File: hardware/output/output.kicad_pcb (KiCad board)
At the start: 2 copper layers, 59.5 x 100 mm, 100 parts, among them J1 AudioJack2_SwitchT, J2 AudioJack2_SwitchT, J3 AudioJack2_SwitchT, J4 AudioJack2_SwitchT, J5 Conn_02x08_Odd_Even, J6 AudioJack3, J7 Conn_02x08_Odd_Even, J8 Conn_02x08_Odd_Even, Q1 2N3906, Q2 2N3904, Q3 2N3906, Q4 2N3904, U1 TL074, U2 LM386, U3 LM386

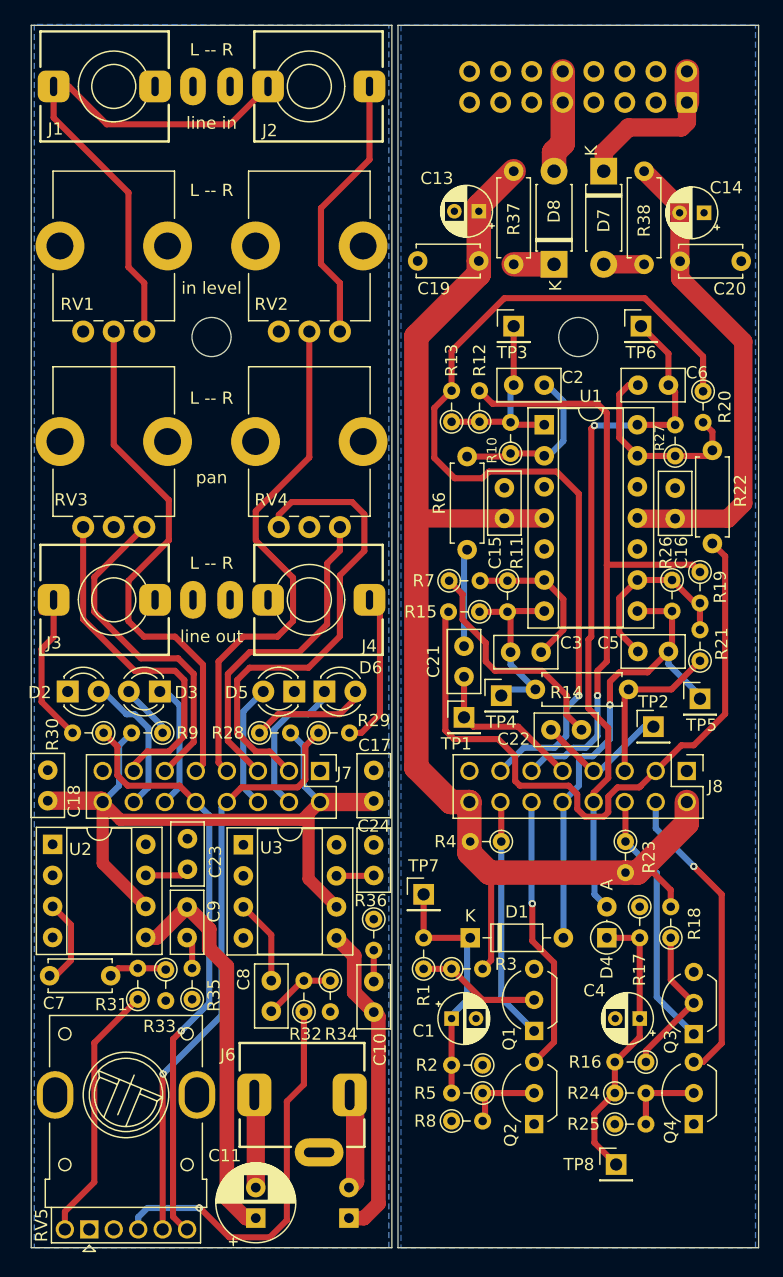
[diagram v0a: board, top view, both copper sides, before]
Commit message: v2 board: SMT components, upgraded OPA1688 amplifier
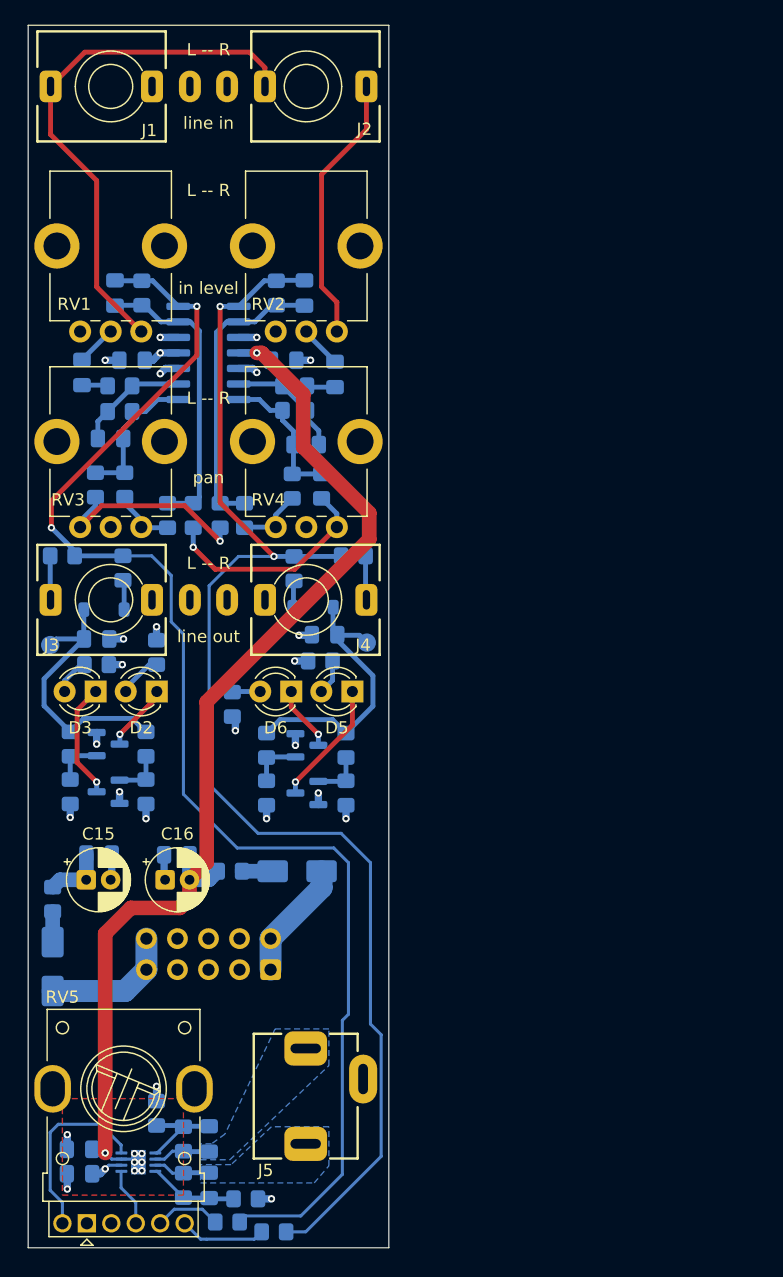
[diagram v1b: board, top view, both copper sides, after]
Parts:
- removed C19, C20: 100n, Capacitor_THT:C_Disc_D5.0mm_W2.5mm_P5.00mm
- removed C21, C22: 1u, Capacitor_THT:C_Disc_D5.0mm_W2.5mm_P2.50mm
- removed C23, C24: 100n, Capacitor_THT:C_Disc_D5.0mm_W2.5mm_P2.50mm
- removed H1, H2: MountingHole, MountingHole:MountingHole_3.2mm_M3_DIN965
- removed the J5 at (153.9, 36.3)
- removed J7, J8: Conn_02x08_Odd_Even, Custom_PinHeader_P2.54mm:PinHeader_2x08_P2.54mm_Vertical_ThinPad
- removed TP3, TP4, TP5, TP6, TP7, TP8: TestPoint, Connector_PinHeader_2.54mm:PinHeader_1x01_P2.54mm_Vertical
- removed U3: LM386, Package_DIP:DIP-8_W7.62mm_Socket
- added J6: Conn_02x05_Odd_Even, Connector_IDC:IDC-Header_2x05_P2.54mm_Vertical, B.Cu at (119.8, 107.3)
- C1: value 10u -> 1u; footprint Capacitor_THT:CP_Radial_D4.0mm_P2.00mm -> Capacitor_SMD:C_0805_2012Metric_Pad1.18x1.45mm_HandSolder; moved to B.Cu
- C10, C9: value 47n -> 100n; footprint Capacitor_THT:C_Disc_D5.0mm_W2.5mm_P2.50mm -> Capacitor_SMD:C_0805_2012Metric_Pad1.18x1.45mm_HandSolder; moved to B.Cu
- C11: value 220u -> 100n; footprint Capacitor_THT:CP_Radial_D6.3mm_P2.50mm -> Capacitor_SMD:C_0805_2012Metric_Pad1.18x1.45mm_HandSolder; moved to B.Cu
- C12: value 220u -> 100n; footprint Capacitor_THT:CP_Radial_D6.3mm_P2.50mm -> Capacitor_SMD:C_0805_2012Metric_Pad1.18x1.45mm_HandSolder
- C13, C14: value 10u -> 100n; footprint Capacitor_THT:CP_Radial_D4.0mm_P2.00mm -> Capacitor_SMD:C_0805_2012Metric_Pad1.18x1.45mm_HandSolder; moved to B.Cu
- C15, C16: value 100n -> 10u; footprint Capacitor_THT:C_Disc_D5.0mm_W2.5mm_P2.50mm -> Capacitor_THT:CP_Radial_D5.0mm_P2.00mm
- C17, C18: value 100n -> 47p; footprint Capacitor_THT:C_Disc_D5.0mm_W2.5mm_P2.50mm -> Capacitor_SMD:C_0805_2012Metric_Pad1.18x1.45mm_HandSolder; moved to B.Cu
- C2: value 22p -> 1u; footprint Capacitor_THT:C_Disc_D5.0mm_W2.5mm_P2.50mm -> Capacitor_SMD:C_0805_2012Metric_Pad1.18x1.45mm_HandSolder; moved to B.Cu
- C3, C5, C6: footprint Capacitor_THT:C_Disc_D5.0mm_W2.5mm_P2.50mm -> Capacitor_SMD:C_0805_2012Metric_Pad1.18x1.45mm_HandSolder; moved to B.Cu
- C4: value 10u -> 22p; footprint Capacitor_THT:CP_Radial_D4.0mm_P2.00mm -> Capacitor_SMD:C_0805_2012Metric_Pad1.18x1.45mm_HandSolder; moved to B.Cu
- C7: value 1u -> 10u; footprint Capacitor_THT:C_Disc_D5.0mm_W2.5mm_P5.00mm -> Capacitor_SMD:C_0805_2012Metric_Pad1.18x1.45mm_HandSolder; moved to B.Cu
- C8: value 1u -> 10u; footprint Capacitor_THT:C_Disc_D5.0mm_W2.5mm_P2.50mm -> Capacitor_SMD:C_0805_2012Metric_Pad1.18x1.45mm_HandSolder; moved to B.Cu
- D1: value 1N4148 -> 1N4148W; footprint Diode_THT:D_DO-35_SOD27_P7.62mm_Horizontal -> Diode_SMD:D_SOD-123; moved to B.Cu
- D2, D5: value GREEN -> RED
- D3, D6: value RED -> GREEN
- D4: value 1N4148 -> 1N4148W; footprint Diode_THT:D_DO-35_SOD27_P2.54mm_Vertical_AnodeUp -> Diode_SMD:D_SOD-123; moved to B.Cu
- D7, D8: value D_Schottky -> B140-E3; footprint Diode_THT:D_DO-41_SOD81_P7.62mm_Horizontal -> Diode_SMD:D_SMA; moved to B.Cu
- J1, J2, J3, J4: footprint AudioJacks:Jack_3.5mm_QingPu_WQP-PJ301M-12_Vertical -> AudioJacks:Jack_3.5mm_QingPu_WQP-PJ301M-12_Vertical_Slim
- Q1, Q3: value 2N3906 -> BC847; footprint Package_TO_SOT_THT:TO-92_Inline_Wide -> Package_TO_SOT_SMD:SOT-23; moved to B.Cu
- Q2, Q4: value 2N3904 -> BC847; footprint Package_TO_SOT_THT:TO-92_Inline_Wide -> Package_TO_SOT_SMD:SOT-23; moved to B.Cu
- R1, R12, R20, R23, R5, R7: footprint Resistor_THT:R_Axial_DIN0204_L3.6mm_D1.6mm_P2.54mm_Vertical -> Resistor_SMD:R_0805_2012Metric_Pad1.20x1.40mm_HandSolder; moved to B.Cu
- R10, R11: value 220k -> 100k; footprint Resistor_THT:R_Axial_DIN0204_L3.6mm_D1.6mm_P2.54mm_Vertical -> Resistor_SMD:R_0805_2012Metric_Pad1.20x1.40mm_HandSolder; moved to B.Cu
- R13: value 100k -> 330k; footprint Resistor_THT:R_Axial_DIN0204_L3.6mm_D1.6mm_P2.54mm_Vertical -> Resistor_SMD:R_0805_2012Metric_Pad1.20x1.40mm_HandSolder; moved to B.Cu
- R14: value 100k -> 330k; footprint Resistor_THT:R_Axial_DIN0207_L6.3mm_D2.5mm_P7.62mm_Horizontal -> Resistor_SMD:R_0805_2012Metric_Pad1.20x1.40mm_HandSolder; moved to B.Cu
- R15, R16: value 100k -> 150k; footprint Resistor_THT:R_Axial_DIN0204_L3.6mm_D1.6mm_P2.54mm_Vertical -> Resistor_SMD:R_0805_2012Metric_Pad1.20x1.40mm_HandSolder; moved to B.Cu
- R17: value 47k -> 1k; footprint Resistor_THT:R_Axial_DIN0204_L3.6mm_D1.6mm_P2.54mm_Vertical -> Resistor_SMD:R_0805_2012Metric_Pad1.20x1.40mm_HandSolder; moved to B.Cu
- R18: value 2M2 -> 1k; footprint Resistor_THT:R_Axial_DIN0204_L3.6mm_D1.6mm_P2.54mm_Vertical -> Resistor_SMD:R_0805_2012Metric_Pad1.20x1.40mm_HandSolder; moved to B.Cu
- R19: value 100k -> 1k; footprint Resistor_THT:R_Axial_DIN0204_L3.6mm_D1.6mm_P2.54mm_Vertical -> Resistor_SMD:R_0805_2012Metric_Pad1.20x1.40mm_HandSolder; moved to B.Cu
- R2: value 47k -> 100k; footprint Resistor_THT:R_Axial_DIN0204_L3.6mm_D1.6mm_P2.54mm_Vertical -> Resistor_SMD:R_0805_2012Metric_Pad1.20x1.40mm_HandSolder; moved to B.Cu
- R21, R24, R31: value 100k -> 22k; footprint Resistor_THT:R_Axial_DIN0204_L3.6mm_D1.6mm_P2.54mm_Vertical -> Resistor_SMD:R_0805_2012Metric_Pad1.20x1.40mm_HandSolder; moved to B.Cu
- R22: value 100k -> 47k; footprint Resistor_THT:R_Axial_DIN0207_L6.3mm_D2.5mm_P7.62mm_Horizontal -> Resistor_SMD:R_0805_2012Metric_Pad1.20x1.40mm_HandSolder; moved to B.Cu
- R25: value 15k -> 10k; footprint Resistor_THT:R_Axial_DIN0204_L3.6mm_D1.6mm_P2.54mm_Vertical -> Resistor_SMD:R_0805_2012Metric_Pad1.20x1.40mm_HandSolder; moved to B.Cu
- R26: value 330k -> 1k; footprint Resistor_THT:R_Axial_DIN0204_L3.6mm_D1.6mm_P2.54mm_Vertical -> Resistor_SMD:R_0805_2012Metric_Pad1.20x1.40mm_HandSolder; moved to B.Cu
- R27: value 330k -> 100k; footprint Resistor_THT:R_Axial_DIN0204_L3.6mm_D1.6mm_P2.54mm_Vertical -> Resistor_SMD:R_0805_2012Metric_Pad1.20x1.40mm_HandSolder; moved to B.Cu
- R28: value 10k -> 22k; footprint Resistor_THT:R_Axial_DIN0204_L3.6mm_D1.6mm_P2.54mm_Vertical -> Resistor_SMD:R_0805_2012Metric_Pad1.20x1.40mm_HandSolder; moved to B.Cu
- R29: value 1k -> 47k; footprint Resistor_THT:R_Axial_DIN0204_L3.6mm_D1.6mm_P2.54mm_Vertical -> Resistor_SMD:R_0805_2012Metric_Pad1.20x1.40mm_HandSolder; moved to B.Cu
- R3: value 2M2 -> 220k; footprint Resistor_THT:R_Axial_DIN0204_L3.6mm_D1.6mm_P2.54mm_Vertical -> Resistor_SMD:R_0805_2012Metric_Pad1.20x1.40mm_HandSolder; moved to B.Cu
- R30: value 1k -> 10k; footprint Resistor_THT:R_Axial_DIN0204_L3.6mm_D1.6mm_P2.54mm_Vertical -> Resistor_SMD:R_0805_2012Metric_Pad1.20x1.40mm_HandSolder; moved to B.Cu
- R32: value 100k -> 10k; footprint Resistor_THT:R_Axial_DIN0204_L3.6mm_D1.6mm_P2.54mm_Vertical -> Resistor_SMD:R_0805_2012Metric_Pad1.20x1.40mm_HandSolder; moved to B.Cu
- R33, R34: value 4k7 -> 10; footprint Resistor_THT:R_Axial_DIN0204_L3.6mm_D1.6mm_P2.54mm_Vertical -> Resistor_SMD:R_0805_2012Metric_Pad1.20x1.40mm_HandSolder; moved to B.Cu
- R35: value 10 -> 0R0; footprint Resistor_THT:R_Axial_DIN0204_L3.6mm_D1.6mm_P2.54mm_Vertical -> Resistor_SMD:R_0805_2012Metric_Pad1.20x1.40mm_HandSolder; moved to B.Cu
- R36: value 10 -> 1k0; footprint Resistor_THT:R_Axial_DIN0204_L3.6mm_D1.6mm_P2.54mm_Vertical -> Resistor_SMD:R_0805_2012Metric_Pad1.20x1.40mm_HandSolder; moved to B.Cu
- R37: value 10 -> 0R0; footprint Resistor_THT:R_Axial_DIN0207_L6.3mm_D2.5mm_P7.62mm_Horizontal -> Resistor_SMD:R_0805_2012Metric_Pad1.20x1.40mm_HandSolder; moved to B.Cu
- R38: value 10 -> 1k0; footprint Resistor_THT:R_Axial_DIN0207_L6.3mm_D2.5mm_P7.62mm_Horizontal -> Resistor_SMD:R_0805_2012Metric_Pad1.20x1.40mm_HandSolder; moved to B.Cu
- R4: value 10k -> 220k; footprint Resistor_THT:R_Axial_DIN0204_L3.6mm_D1.6mm_P2.54mm_Vertical -> Resistor_SMD:R_0805_2012Metric_Pad1.20x1.40mm_HandSolder; moved to B.Cu
- R6: footprint Resistor_THT:R_Axial_DIN0207_L6.3mm_D2.5mm_P7.62mm_Horizontal -> Resistor_SMD:R_0805_2012Metric_Pad1.20x1.40mm_HandSolder; moved to B.Cu
- R8: value 15k -> 100k; footprint Resistor_THT:R_Axial_DIN0204_L3.6mm_D1.6mm_P2.54mm_Vertical -> Resistor_SMD:R_0805_2012Metric_Pad1.20x1.40mm_HandSolder; moved to B.Cu
- R9: value 10k -> 100k; footprint Resistor_THT:R_Axial_DIN0204_L3.6mm_D1.6mm_P2.54mm_Vertical -> Resistor_SMD:R_0805_2012Metric_Pad1.20x1.40mm_HandSolder; moved to B.Cu
- TP1, TP2: footprint Connector_PinHeader_2.54mm:PinHeader_1x01_P2.54mm_Vertical -> TestPoint:TestPoint_Pad_D1.5mm; moved to B.Cu
- U1: footprint Package_DIP:DIP-14_W7.62mm_Socket -> Package_SO:SOIC-14_3.9x8.7mm_P1.27mm; moved to B.Cu
- U2: value LM386 -> OPA1688IDRG; footprint Package_DIP:DIP-8_W7.62mm_Socket -> Package_SON:WSON-8-1EP_3x3mm_P0.5mm_EP1.2x2mm; moved to B.Cu
- moved R38 86.8 mm to (110.5, 119.0), turned to 90 degrees
- moved R37 83.6 mm to (112.7, 121.1), turned to 90 degrees
- moved D7 79.2 mm to (102.0, 107.0)
- moved C14 68.0 mm to (112.2, 97.9)
- moved C13 61.1 mm to (105.8, 97.8)
- moved C1 60.9 mm to (104.4, 58.4), turned to -90 degrees
- moved R20 59.3 mm to (103.4, 88.8), turned to 90 degrees
- moved R5 57.7 mm to (107.9, 67.6), turned to -90 degrees
- moved R2 57.7 mm to (121.8, 59.5)
- moved R25 56.7 mm to (105.6, 82.3), turned to 180 degrees
- moved R17 55.3 mm to (102.8, 73.4), turned to 180 degrees
- moved C4 54.3 mm to (122.7, 64.3)
- moved R15 54.0 mm to (116.3, 127.9)
- moved D8 53.9 mm to (122.0, 99.2), turned to 180 degrees
- moved C10 53.8 mm to (120.9, 57.4), turned to 0 degrees
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- renumbered J6 to J5
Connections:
- C1 pad 1: Net-(D1-K) -> Net-(C1-Pad1)
- C1 pad 2: GND -> Net-(C1-Pad2)
- C10 pad 1: Net-(C10-Pad1) -> -12V
- C10 pad 2: Net-(C10-Pad2) -> GND
- C11 pad 1: Net-(C11-Pad1) -> GND
- C11 pad 2: Net-(C11-Pad2) -> +12V
- C12 pad 1: Net-(C10-Pad1) -> -12V
- C12 pad 2: Net-(C12-Pad2) -> GND
- C13 pad 1: +12V -> GND
- C13 pad 2: GND -> +12V
- C14 pad 1: GND -> -12V
- C14 pad 2: -12V -> GND
- C15 pad 1: GND -> +12V
- C15 pad 2: +12V -> GND
- C16 pad 1: -12V -> GND
- C16 pad 2: GND -> -12V
- C17 pad 1: GND -> Net-(U2A--)
- C17 pad 2: +12V -> /L_HP_OUT
- C18 pad 1: GND -> Net-(U2B--)
- C18 pad 2: +12V -> /R_HP_OUT
- C2 pad 1: Net-(U1A--) -> Net-(C2-Pad1)
- C3 pad 1: Net-(U1B--) -> Net-(U1A--)
- C4 pad 1: Net-(D4-K) -> Net-(U1D--)
- C4 pad 2: GND -> Net-(C4-Pad2)
- C5 pad 1: Net-(U1C--) -> Net-(U1B--)
- C5 pad 2: L_LINE_OUT_B -> /L_LINE_OUT
- C6 pad 1: Net-(U1D--) -> Net-(U1C--)
- C6 pad 2: R_LINE_OUT_B -> /R_LINE_OUT
- C7 pad 1: Net-(U2-+) -> GND
- C7 pad 2: Net-(C7-Pad2) -> Net-(D1-K)
- C8 pad 1: Net-(U3-+) -> GND
- C8 pad 2: Net-(C8-Pad2) -> Net-(D4-K)
- C9 pad 1: Net-(C11-Pad1) -> GND
- C9 pad 2: Net-(C9-Pad2) -> +12V
- D1 pad 2: L_LINE_OUT_B -> Net-(D1-A)
- D2 pad 1: GND -> Net-(D2-K)
- D2 pad 2: L_LVL_G_LED_A -> Net-(D2-A)
- D3 pad 1: L_LVL_R_LED_A -> Net-(D3-K)
- D4 pad 2: R_LINE_OUT_B -> Net-(D4-A)
- D5 pad 1: GND -> Net-(D5-K)
- D5 pad 2: R_LVL_G_LED_A -> Net-(D5-A)
- D6 pad 1: R_LVL_R_LED_A -> Net-(D6-K)
- J5 pad R: Net-(C12-Pad2) -> /R_HP_OUT
- J5 pad T: Net-(C11-Pad2) -> /L_HP_OUT
- Q1 pad 1: L_LVL_G_LED_B -> Net-(Q1-B)
- Q1 pad 2: Net-(Q1-B) -> GND
- Q1 pad 3: GND -> Net-(D2-K)
- Q2 pad 1: GND -> Net-(Q2-B)
- Q2 pad 2: Net-(Q2-B) -> GND
- Q2 pad 3: L_LVL_R_LED_B -> Net-(D3-K)
- Q3 pad 1: R_LVL_G_LED_B -> Net-(Q3-B)
- Q3 pad 2: Net-(Q3-B) -> GND
- Q3 pad 3: GND -> Net-(D5-K)
- Q4 pad 1: GND -> Net-(Q4-B)
- Q4 pad 2: Net-(Q4-B) -> GND
- Q4 pad 3: R_LVL_R_LED_B -> Net-(D6-K)
- R1 pad 1: Net-(Q1-B) -> Net-(C1-Pad2)
- R1 pad 2: Net-(D1-K) -> Net-(U1A--)
- R10 pad 1: Net-(U1A--) -> Net-(R10-Pad1)
- R10 pad 2: Net-(C2-Pad2) -> Net-(U1C--)
- R11 pad 1: Net-(U1B--) -> Net-(R11-Pad1)
- R11 pad 2: Net-(C3-Pad2) -> Net-(U1B--)
- R12 pad 1: Net-(C2-Pad2) -> Net-(R12-Pad1)
- R12 pad 2: L_PAN_1_B -> Net-(U1C--)
- R13 pad 1: Net-(C2-Pad2) -> Net-(U1B--)
- R13 pad 2: L_PAN_2_B -> /L_LINE_OUT
- R14 pad 1: Net-(C3-Pad2) -> Net-(U1C--)
- R14 pad 2: R_PAN_1_B -> /R_LINE_OUT
- R15 pad 1: Net-(C3-Pad2) -> /L_LINE_OUT
- R15 pad 2: R_PAN_2_B -> Net-(R15-Pad2)
- R16 pad 1: Net-(Q3-B) -> /R_LINE_OUT
- R16 pad 2: Net-(D4-K) -> Net-(R16-Pad2)
- R17 pad 1: GND -> /L_LINE_OUT
- R17 pad 2: Net-(D4-K) -> Net-(J3-PadT)
- R18 pad 1: Net-(Q3-B) -> /R_LINE_OUT
- R18 pad 2: +12V -> Net-(J4-PadT)
- R19 pad 1: L_PAN_1_B -> Net-(D1-A)
- R19 pad 2: Net-(U1C--) -> /L_LINE_OUT
- R2 pad 1: GND -> Net-(C2-Pad2)
- R2 pad 2: Net-(D1-K) -> Net-(U1D--)
- R20 pad 1: L_PAN_2_B -> Net-(Q1-B)
- R20 pad 2: Net-(U1D--) -> Net-(D1-K)
- R21 pad 1: R_PAN_1_B -> GND
- R21 pad 2: Net-(U1C--) -> Net-(Q1-B)
- R22 pad 1: R_PAN_2_B -> Net-(Q2-B)
- R22 pad 2: Net-(U1D--) -> Net-(D1-K)
- R23 pad 1: R_LVL_G_LED_B -> +12V
- R23 pad 2: +12V -> Net-(D2-A)
- R24 pad 1: Net-(D4-K) -> GND
- R24 pad 2: Net-(Q4-B) -> Net-(Q2-B)
- R25 pad 1: GND -> +12V
- R25 pad 2: Net-(Q4-B) -> Net-(D3-A)
- R26 pad 1: Net-(U1C--) -> Net-(D4-A)
- R26 pad 2: L_LINE_OUT_B -> /R_LINE_OUT
- R27 pad 1: Net-(U1D--) -> Net-(Q3-B)
- R27 pad 2: R_LINE_OUT_B -> Net-(D4-K)
- R28 pad 1: Net-(D6-A) -> GND
- R28 pad 2: +12V -> Net-(Q3-B)
- R29 pad 1: R_LINE_OUT_A -> Net-(Q4-B)
- R29 pad 2: Net-(J4-PadT) -> Net-(D4-K)
- R3 pad 1: Net-(Q1-B) -> Net-(U1A--)
- R3 pad 2: +12V -> Net-(C3-Pad2)
- R30 pad 1: L_LINE_OUT_A -> +12V
- R30 pad 2: Net-(J3-PadT) -> Net-(D5-A)
- R31 pad 1: Net-(R31-Pad1) -> GND
- R31 pad 2: Net-(C7-Pad2) -> Net-(Q4-B)
- R32 pad 1: Net-(R32-Pad1) -> +12V
- R32 pad 2: Net-(C8-Pad2) -> Net-(D6-A)
- R33 pad 1: Net-(C7-Pad2) -> +12V
- R33 pad 2: GND -> Net-(D7-K)
- R34 pad 1: Net-(C8-Pad2) -> -12V
- R34 pad 2: GND -> Net-(D8-A)
- R35 pad 1: GND -> /L_HP_OUT
- R35 pad 2: Net-(C9-Pad2) -> Net-(U2A--)
- R36 pad 1: GND -> Net-(U2A--)
- R36 pad 2: Net-(C10-Pad2) -> GND
- R37 pad 1: +12V -> /R_HP_OUT
- R37 pad 2: Net-(D8-K) -> Net-(U2B--)
- R38 pad 1: -12V -> Net-(U2B--)
- R38 pad 2: Net-(D7-A) -> GND
- R4 pad 1: L_LVL_G_LED_B -> Net-(U1D--)
- R4 pad 2: +12V -> Net-(C4-Pad2)
- R5 pad 1: Net-(Q2-B) -> Net-(C3-Pad2)
- R5 pad 2: Net-(D1-K) -> Net-(R5-Pad2)
- R6 pad 1: Net-(C21-Pad2) -> Net-(C3-Pad2)
- R6 pad 2: Net-(U1A--) -> Net-(R10-Pad1)
- R7 pad 1: Net-(C22-Pad2) -> Net-(C4-Pad2)
- R7 pad 2: Net-(U1B--) -> Net-(R11-Pad1)
- R8 pad 1: GND -> Net-(C4-Pad2)
- R8 pad 2: Net-(Q2-B) -> Net-(R12-Pad1)
- R9 pad 1: Net-(D3-A) -> Net-(R5-Pad2)
- R9 pad 2: +12V -> Net-(U1B--)
- RV1 pad : (no net) -> GND
- RV1 pad 2: L_LINE_IN_A -> Net-(C1-Pad1)
- RV2 pad : (no net) -> GND
- RV2 pad 2: R_LINE_IN_A -> Net-(C2-Pad1)
- RV3 pad : (no net) -> GND
- RV3 pad 1: L_PAN_1_A -> Net-(R5-Pad2)
- RV3 pad 3: L_PAN_2_A -> Net-(R10-Pad1)
- RV4 pad : (no net) -> GND
- RV4 pad 1: R_PAN_1_A -> Net-(R11-Pad1)
- RV4 pad 3: R_PAN_2_A -> Net-(R12-Pad1)
- RV5 pad 2: Net-(R31-Pad1) -> Net-(U2B-+)
- RV5 pad 3: L_LINE_OUT_A -> Net-(R16-Pad2)
- RV5 pad 5: Net-(R32-Pad1) -> Net-(U2A-+)
- RV5 pad 6: R_LINE_OUT_A -> Net-(R15-Pad2)
- RV5 pad SH: (no net) -> GND
- TP1 pad 1: L_LINE_IN_B -> Net-(D1-K)
- TP2 pad 1: R_LINE_IN_B -> Net-(D4-K)
- U1 pad 1: Net-(C2-Pad2) -> Net-(C3-Pad2)
- U1 pad 14: R_LINE_OUT_B -> Net-(C4-Pad2)
- U1 pad 7: Net-(C3-Pad2) -> /L_LINE_OUT
- U1 pad 8: L_LINE_OUT_B -> /R_LINE_OUT
- U2 pad 1: unconnected-(U2-GAIN-Pad1) -> Net-(U2A-+)
- U2 pad 2: GND -> +12V
- U2 pad 3: Net-(U2-+) -> -12V
- U2 pad 4: GND -> Net-(U2B-+)
- U2 pad 5: Net-(C11-Pad1) -> Net-(U2B--)
- U2 pad 6: +12V -> /R_HP_OUT
- U2 pad 7: Net-(U2-BYPASS) -> /L_HP_OUT
- U2 pad 8: unconnected-(U2-GAIN-Pad8) -> Net-(U2A--)
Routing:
- net +12V: track 172.2 -> 15.3 mm, vias 0 -> 6
- net /L_LINE_OUT: track 0.00 -> 112.1 mm, vias 0 -> 2
- net /R_LINE_OUT: track 0.00 -> 108.7 mm, vias 0 -> 2
- net L_PAN_2_B: track 76.8 -> 0.00 mm, vias 1 -> 0
- net R_LINE_OUT_B: track 57.2 -> 0.00 mm, vias 1 -> 0
- net R_PAN_2_B: track 56.1 -> 0.00 mm
- net L_PAN_1_B: track 52.4 -> 0.00 mm, vias 1 -> 0
- net R_LINE_OUT_A: track 48.7 -> 0.00 mm, vias 1 -> 0
- net L_LINE_OUT_A: track 48.5 -> 0.00 mm, vias 1 -> 0
- net -12V: track 47.7 -> 92.5 mm, vias 0 -> 8
- net R_LINE_IN_A: track 43.5 -> 0.00 mm
- net L_LINE_IN_A: track 43.4 -> 0.00 mm
- net L_LINE_OUT_B: track 39.7 -> 0.00 mm, vias 1 -> 0
- net R_PAN_2_A: track 39.4 -> 0.00 mm
- net Net-(R32-Pad1): track 32.9 -> 0.00 mm, vias 1 -> 0
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- added copper zone on In1.Cu, net +12V
- added copper zone on F.Cu, net -12V
- added copper zone on B.Cu, net /L_HP_OUT
- added copper zone on B.Cu, net /R_HP_OUT
- added copper zone on In2.Cu, net GND
- removed copper zone on B.Cu, net GND
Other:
- board size 59.5 x 100 mm -> 29.5 x 100 mm
- copper layers 2 -> 4
- board text added: "OUTPUT"
- board text added: "idyllm CC BY-SA 4.0"
- board text added: "v2.0.20261019"
- board text removed: "OUTPUT-1"
- board text removed: "idyllm"
- board text removed: "v1.1.20240910 CC BY-SA 4.0"
